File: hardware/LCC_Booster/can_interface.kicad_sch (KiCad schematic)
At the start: 10 parts, among them U11 MCP2518FD-xQBB, U12 MCP2562-E-SN, Y1 ECS-400-20-46X

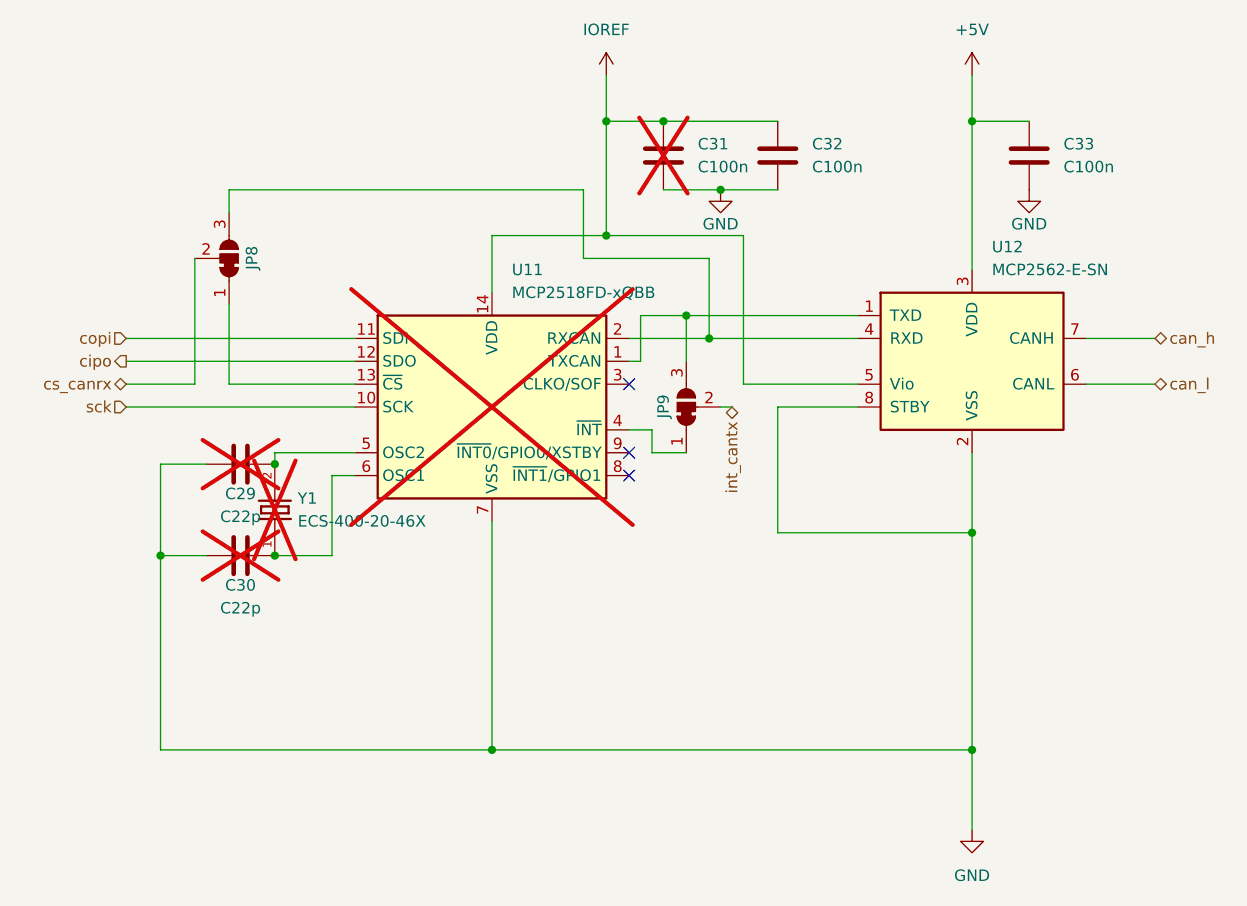
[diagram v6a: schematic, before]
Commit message: Add Fault Pin Inputs to Arduino
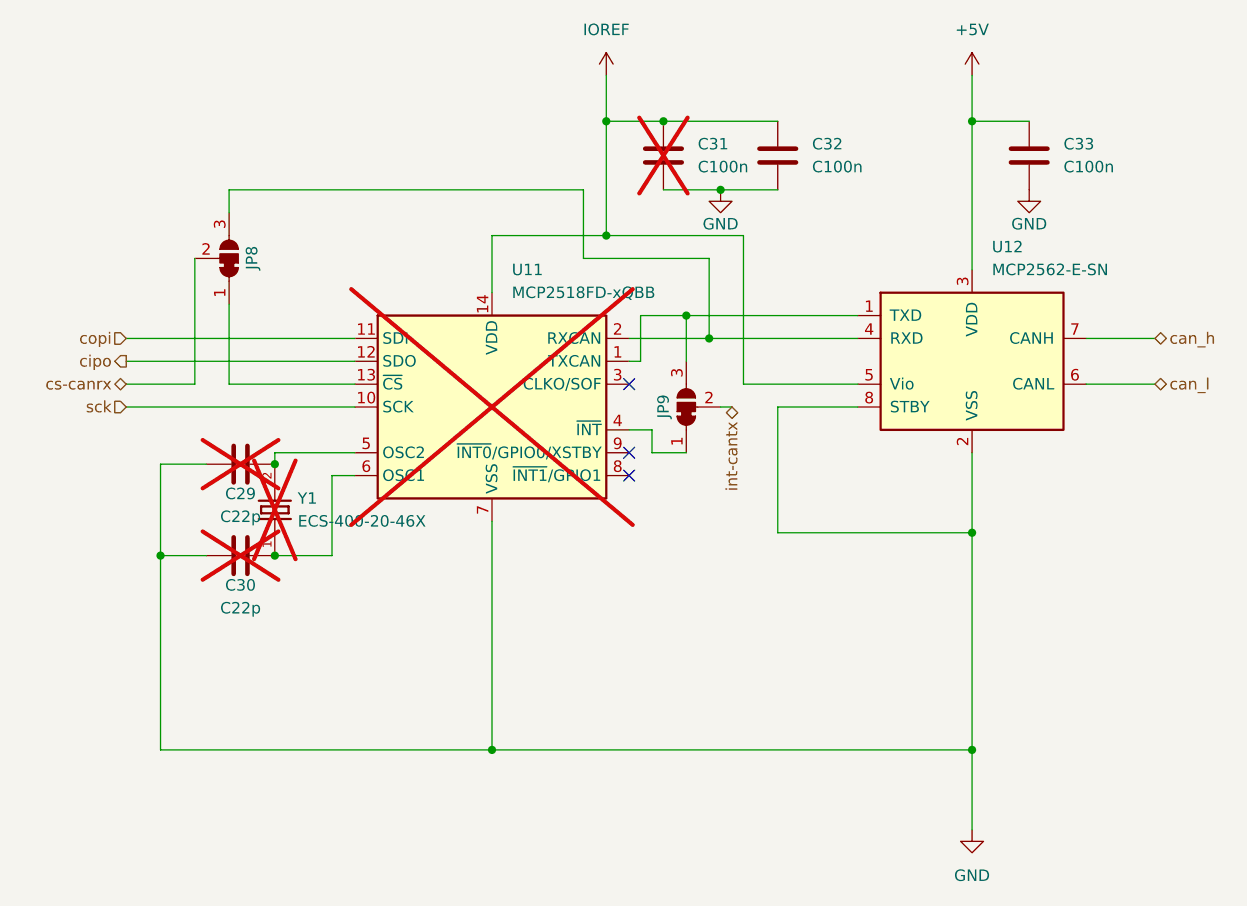
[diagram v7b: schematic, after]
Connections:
- net cs_canrx renamed cs-canrx
- net int_cantx renamed int-cantx
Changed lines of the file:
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@@
 	(title_block
 		(title "Arduino Nano LCC Booster")
-		(date "2024-05-14")
-		(rev "2")
+		(date "2024-09-10")
+		(rev "4")
 		(company "TMRC")
 		(comment 1 "Noah Paladino")
@@
 		)
 	)
-	(hierarchical_label "cs_canrx"
+	(hierarchical_label "cs-canrx"
 		(shape bidirectional)
 		(at 92.71 82.55 180)
@@
 		)
 	)
-	(hierarchical_label "int_cantx"
+	(hierarchical_label "int-cantx"
 		(shape bidirectional)
 		(at 160.02 85.09 270)

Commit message: Update for PCB Assembly
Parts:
- C32, C33: MANUFACTURER (none) -> Samsung; Manufacturer Part Number (none) -> CL05B104K05NNNC
- U10: renamed from U12; MANUFACTURER (none) -> Microchip; Manufacturer Part Number (none) -> MCP2562-E-SN
- renumbered JP8 to JP10, JP9 to JP11, U11 to U9
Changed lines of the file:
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@@
+			)
+		)
+		(property "Manufacturer Part Number" ""
+			(at 105.41 91.44 0)
+			(effects
+				(font
+					(size 1.27 1.27)
+				)
+				(hide yes)
 			)
 		)
@@
 		(on_board yes)
 		(dnp no)
-		(property "Reference" "JP9"
+		(property "Reference" "JP11"
 			(at 152.4 86.3601 0)
 			(effects
@@
 			)
 		)
+		(property "Manufacturer Part Number" ""
+			(at 154.94 85.09 0)
+			(effects
+				(font
+					(size 1.27 1.27)
+				)
+				(hide yes)
+			)
+		)
 		(pin "1"
 		)
@@
 			(project "LCC_Booster"
 				(path "/e8524381-bb01-4107-93ec-8133e878a3da/b324a729-c370-420a-b992-28ea70226130"
-					(reference "JP9")
+					(reference "JP11")
 					(unit 1)
 				)
@@
 		(on_board yes)
 		(dnp no)
-		(property "Reference" "JP8"
+		(property "Reference" "JP10"
 			(at 106.68 69.8501 0)
 			(effects
@@
 			)
 		)
+		(property "Manufacturer Part Number" ""
+			(at 104.14 68.58 0)
+			(effects
+				(font
+					(size 1.27 1.27)
+				)
+				(hide yes)
+			)
+		)
 		(pin "1"
 		)
@@
 			(project "LCC_Booster"
 				(path "/e8524381-bb01-4107-93ec-8133e878a3da/b324a729-c370-420a-b992-28ea70226130"
-					(reference "JP8")
+					(reference "JP10")
 					(unit 1)
 				)
@@
 			)
 		)
+		(property "Manufacturer Part Number" ""
+			(at 109.22 96.52 0)
+			(effects
+				(font
+					(size 1.27 1.27)
+				)
+				(hide yes)
+			)
+		)
 		(pin "2"
 		)
@@
 		(dnp yes)
 		(fields_autoplaced yes)
-		(property "Reference" "U11"
+		(property "Reference" "U9"
 			(at 135.5441 69.85 0)
 			(effects
@@
 			)
 		)
+		(property "Manufacturer Part Number" ""
+			(at 133.35 85.09 0)
+			(effects
+				(font
+					(size 1.27 1.27)
+				)
+				(hide yes)
+			)
+		)
 		(pin "3"
 		)
@@
 			(project "LCC_Booster"
 				(path "/e8524381-bb01-4107-93ec-8133e878a3da/b324a729-c370-420a-b992-28ea70226130"
-					(reference "U11")
+					(reference "U9")
 					(unit 1)
 				)
@@
 		(dnp no)
 		(fields_autoplaced yes)
-		(property "Reference" "U12"
+		(property "Reference" "U10"
 			(at 188.8841 67.31 0)
 			(effects
@@
 			)
 		)
+		(property "MANUFACTURER" "Microchip"
+			(at 186.69 80.01 0)
+			(effects
+				(font
+					(size 1.27 1.27)
+				)
+				(hide yes)
+			)
+		)
+		(property "Manufacturer Part Number" "MCP2562-E-SN"
+			(at 186.69 80.01 0)
+			(effects
+				(font
+					(size 1.27 1.27)
+				)
+				(hide yes)
+			)
+		)
 		(pin "3"
 		)
@@
 			(project "LCC_Booster"
 				(path "/e8524381-bb01-4107-93ec-8133e878a3da/b324a729-c370-420a-b992-28ea70226130"
-					(reference "U12")
+					(reference "U10")
 					(unit 1)
 				)
@@
 			)
 		)
+		(property "Manufacturer Part Number" ""
+			(at 152.4 57.15 0)
+			(effects
+				(font
+					(size 1.27 1.27)
+				)
+				(hide yes)
+			)
+		)
 		(pin "2"
 		)
@@
 			)
 		)
+		(property "Manufacturer Part Number" ""
+			(at 105.41 101.6 0)
+			(effects
+				(font
+					(size 1.27 1.27)
+				)
+				(hide yes)
+			)
+		)
 		(pin "2"
 		)
@@
 			)
 		)
+		(property "MANUFACTURER" "Samsung"
+			(at 193.04 57.15 0)
+			(effects
+				(font
+					(size 1.27 1.27)
+				)
+				(hide yes)
+			)
+		)
+		(property "Manufacturer Part Number" "CL05B104K05NNNC"
+			(at 193.04 57.15 0)
+			(effects
+				(font
+					(size 1.27 1.27)
+				)
+				(hide yes)
+			)
+		)
 		(pin "2"
 		)
@@
 			(at 165.1 57.15 0)
 			(effects
+				(font
+					(size 1.27 1.27)
+				)
+				(hide yes)
+			)
+		)
+		(property "MANUFACTURER" "Samsung"
+			(at 165.1 57.15 0)
+			(effects
+				(font
+					(size 1.27 1.27)
+				)
+				(hide yes)
+			)
+		)
+		(property "Manufacturer Part Number" "CL05B104K05NNNC"
+			(at 165.1 57.15 0)
+			(effects
